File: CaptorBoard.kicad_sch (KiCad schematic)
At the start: 51 parts, among them J1 Conn_01x06-Connector, J2 Screw_Terminal_01x03, J3 Screw_Terminal_01x03, J4 Conn_01x07, J5 Conn_01x04, J6 Screw_Terminal_01x03, K1 G5LE-1-DC5, K2 G5LE-1-DC5, Q1 2N7002E, Q2 2N7002E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

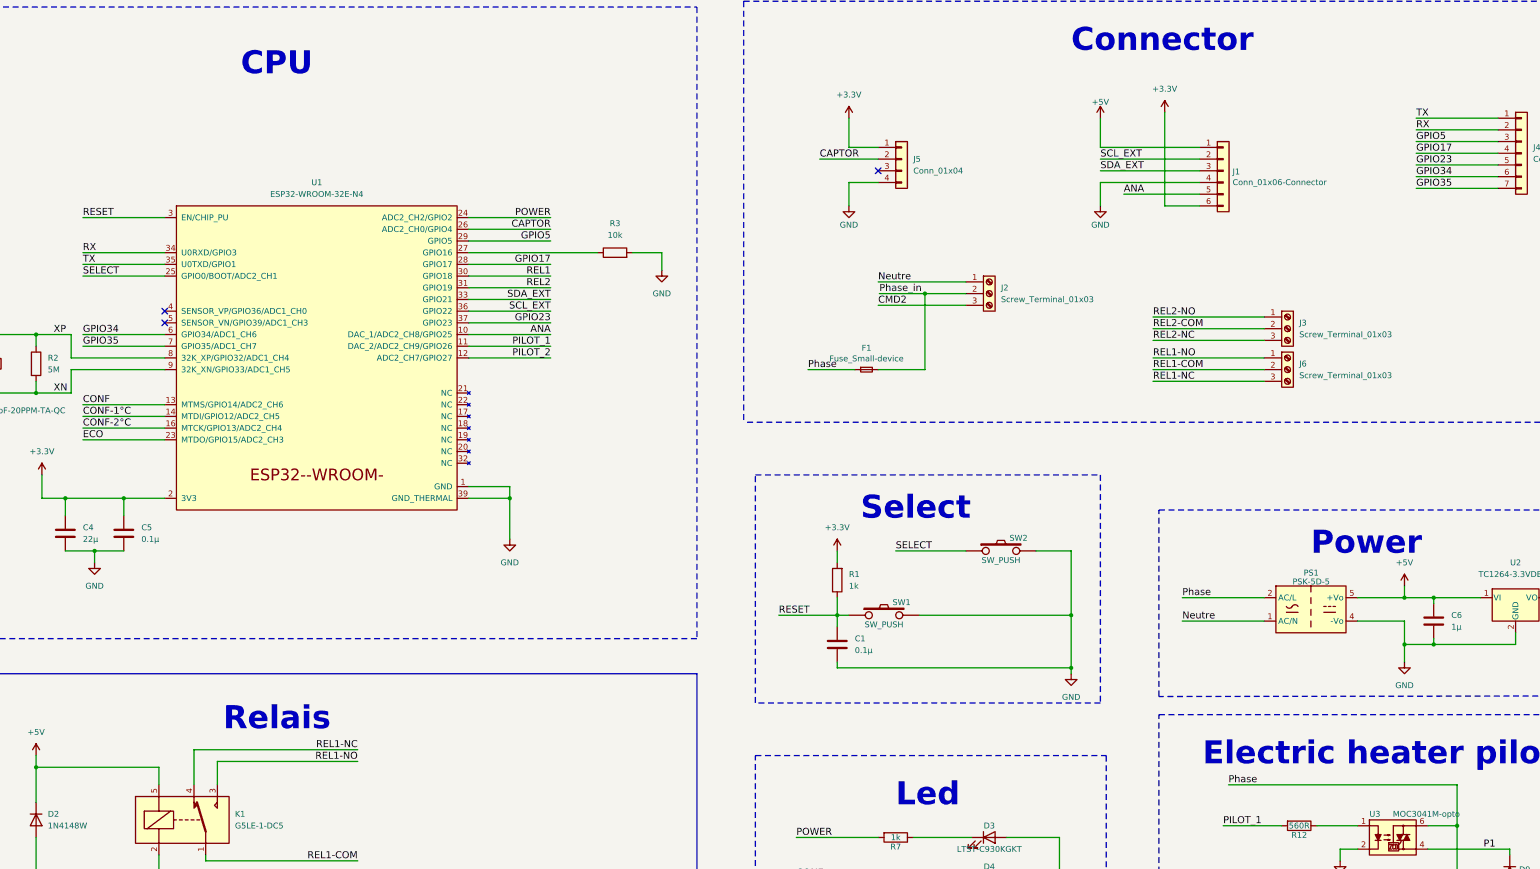
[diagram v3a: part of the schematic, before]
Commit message: Add two more anlog input and protect it
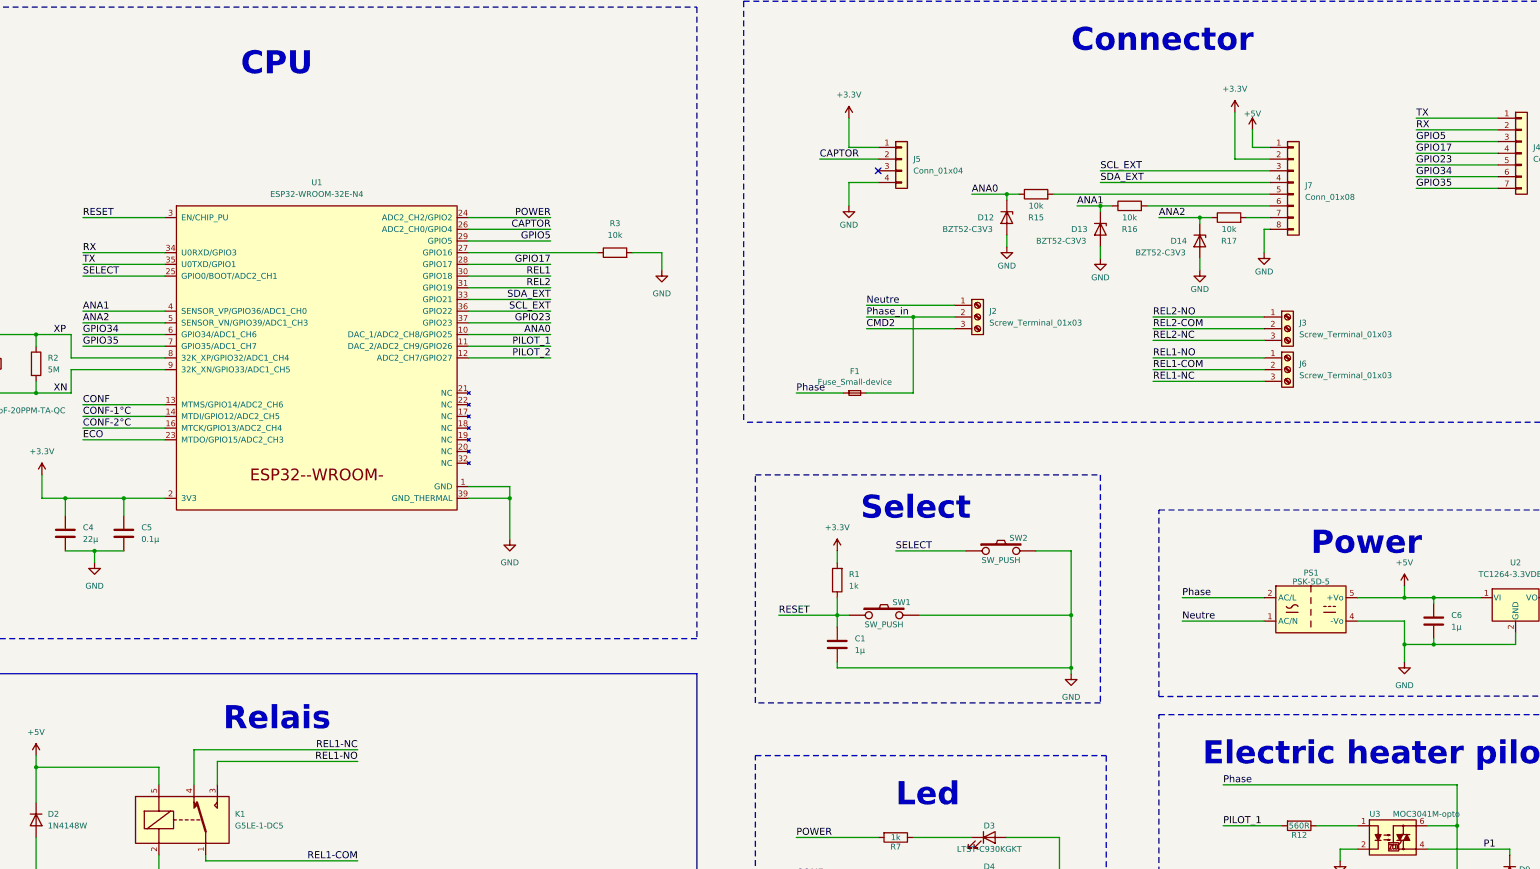
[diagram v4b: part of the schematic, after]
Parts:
- removed J1: Conn_01x06-Connector, Connector_PinHeader_2.54mm:PinHeader_1x06_P2.54mm_Vertical, symbol CaptorBoard-rescue:Conn_01x06-Connector
- added D12, D13, D14: BZT52-C3V3, Diode_SMD:D_SOD-123F, symbol Diode:BZT52Bxx
- added J7: Conn_01x08, Connector_PinHeader_2.54mm:PinHeader_1x08_P2.54mm_Vertical, symbol Connector_Generic:Conn_01x08
- added R15, R16, R17: 10k, Resistor_SMD:R_1210_3225Metric_Pad1.30x2.65mm_HandSolder, symbol Device:R
- C1: value 0.1µ -> 1µ; manf# 12101C104K4T2A -> CL32B105KBHNNNE
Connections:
- net +3.3V: now also J7.2 (Pin_2)
- net +5V: now also J7.1 (Pin_1)
- net GND: now also D12.2 (A), D13.2 (A), D14.2 (A), J7.8 (Pin_8)
- net SCL_EXT: now also J7.3 (Pin_3)
- net SDA_EXT: now also J7.4 (Pin_4)
- net ANA1: now reaches U1.4 (SENSOR_VP/GPIO36/ADC1_CH0)
- net ANA1: now also D13.1 (K), R16.1
- net ANA2: now reaches U1.5 (SENSOR_VN/GPIO39/ADC1_CH3)
- net ANA2: now also D14.1 (K), R17.1
- net ANA renamed ANA0
- net ANA0: now also D12.1 (K), R15.1
- new net: J7.7 (Pin_7), R17.2
- new net: J7.5 (Pin_5), R15.2
- new net: J7.6 (Pin_6), R16.2
- no-connect marks 3 -> 1
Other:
- moved on the sheet: F1, J2

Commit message: Change connecteur and pin for a better routing
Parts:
- removed J4: Conn_01x07, Connector_PinHeader_2.54mm:PinHeader_1x07_P2.54mm_Vertical, symbol Connector_Generic:Conn_01x07
- J7: footprint Connector_PinHeader_2.54mm:PinHeader_1x08_P2.54mm_Vertical -> Connector_PinHeader_2.54mm:PinHeader_2x08_P2.54mm_Vertical; symbol Connector_Generic:Conn_01x08 -> Connector_Generic:Conn_02x08_Odd_Even
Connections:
- net GPIO17 is gone; now on net CONF: U1.28 (GPIO17)
- net GPIO5 is gone; now on net CONF-1°C: U1.29 (GPIO5)
- net +3.3V: now also J7.1 (Pin_1); no longer J7.2 (Pin_2)
- net +5V: now also J7.2 (Pin_2), J7.3 (Pin_3); no longer J7.1 (Pin_1)
- net CONF: no longer U1.13 (MTMS/GPIO14/ADC2_CH6)
- net CONF-1°C: no longer U1.14 (MTDI/GPIO12/ADC2_CH5)
- net CONF-2°C: now also U1.30 (GPIO18); no longer U1.16 (MTCK/GPIO13/ADC2_CH4)
- net ECO: now also U1.31 (GPIO19); no longer U1.23 (MTDO/GPIO15/ADC2_CH3)
- net GND: now also J7.15 (Pin_15); no longer J7.8 (Pin_8)
- net GPIO23: now also J7.12 (Pin_12)
- net GPIO34: now also J7.8 (Pin_8)
- net GPIO35: now also J7.10 (Pin_10)
- net PILOT_1: now also U1.14 (MTDI/GPIO12/ADC2_CH5); no longer U1.11 (DAC_2/ADC2_CH9/GPIO26)
- net PILOT_2: now also U1.13 (MTMS/GPIO14/ADC2_CH6); no longer U1.12 (ADC2_CH7/GPIO27)
- net REL1: now also U1.16 (MTCK/GPIO13/ADC2_CH4); no longer U1.30 (GPIO18)
- net REL2: now also U1.23 (MTDO/GPIO15/ADC2_CH3); no longer U1.31 (GPIO19)
- net RX: now also J7.6 (Pin_6)
- net SCL_EXT: now also J7.5 (Pin_5); no longer J7.3 (Pin_3)
- net SDA_EXT: now also J7.7 (Pin_7); no longer J7.4 (Pin_4)
- net TX: now also J7.4 (Pin_4)
- net at R17.2: now also J7.13 (Pin_13); no longer J7.7 (Pin_7)
- net at R15.2: now also J7.9 (Pin_9); no longer J7.5 (Pin_5)
- net at R16.2: now also J7.11 (Pin_11); no longer J7.6 (Pin_6)
- new net GPIO26: J7.14 (Pin_14), U1.11 (DAC_2/ADC2_CH9/GPIO26)
- new net GPIO27: J7.16 (Pin_16), U1.12 (ADC2_CH7/GPIO27)

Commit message: add CEM protection, and change reférance for Digikey distributor
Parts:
- added R18: 12, Resistor_SMD:R_2512_6332Metric_Pad1.40x3.35mm_HandSolder, symbol Device:R
- added RV1: B72210S0351K101, Varistor:RV_Disc_D12mm_W5.1mm_P7.5mm, symbol Device:Varistor
- C2, C3: footprint Capacitor_SMD:C_1210_3225Metric_Pad1.33x2.70mm_HandSolder -> Capacitor_SMD:C_1206_3216Metric_Pad1.33x1.80mm_HandSolder; manf# C1210C120J1HACTU -> C1206C120J5GAC7800
- D10, D9: manf# 1N4004T-G -> 1N4004RLG
- F1: manf# 0443001.DR -> 3405.0166.11
- PS1: value PSK-5D-5 -> LD03-23B05R2; manf# PSK-5D-5 -> LD03-23B05R2
- Q1, Q2: manf# 2N7002E-7-F -> T2N7002BK\,LM
- R1, R10, R11, R14, R5, R7, R8, R9: manf# RMC1/4-102JTE -> RMCF1210JT1K00
- SW1, SW2: manf# SKHHLPA010 -> TL1105VF100Q
- U1: value ESP32-WROOM-32E-N4 -> ESP32-WROOM-32E-H4; manf# ESP32-WROOM-32E-N4 -> ESP32-WROOM-32E-H4
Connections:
- net Neutre: now also RV1.2
- net Phase: now also R18.1, RV1.1; no longer PS1.2 (AC/L)
- new net Phase_f: PS1.2 (AC/L), R18.2
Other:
- moved on the sheet: C1, C6, D10, D12, D13, D14, D3, D4, D5, D6, D7, D9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

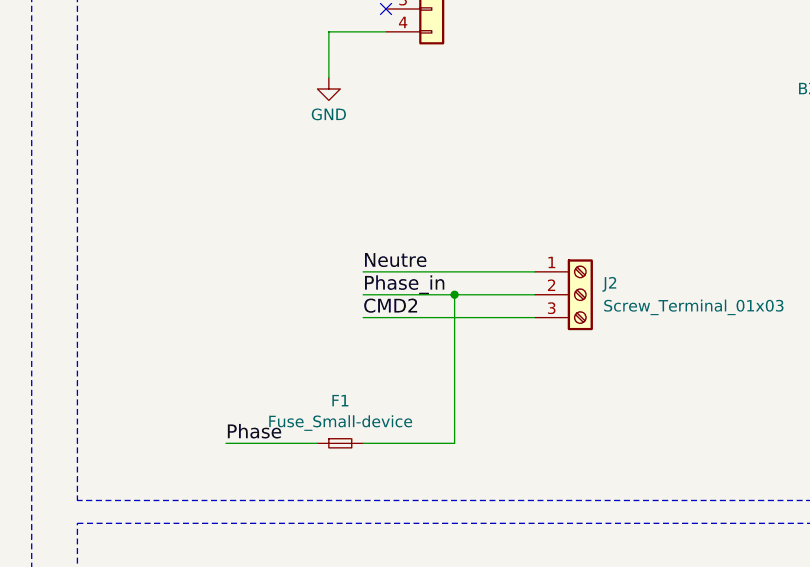
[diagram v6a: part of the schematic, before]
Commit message: change a bad foot print for fuse
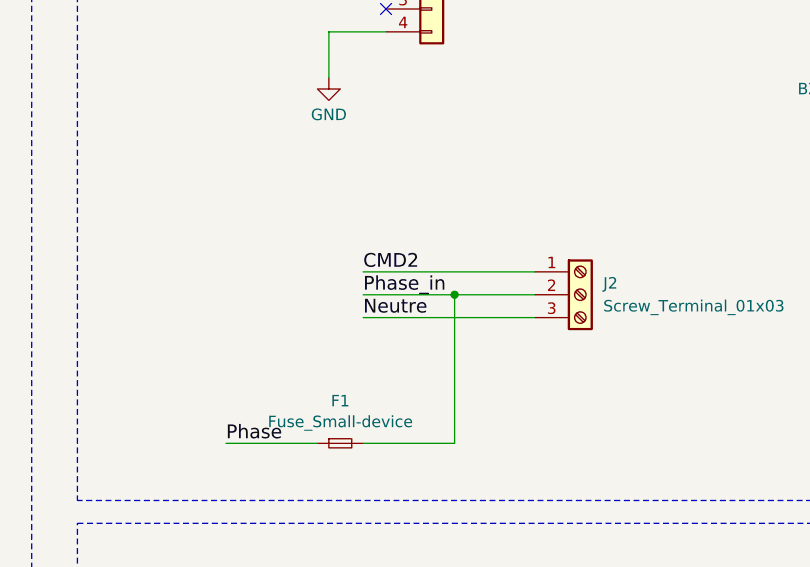
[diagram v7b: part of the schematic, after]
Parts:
- F1: footprint Fuse:Fuseholder_Littelfuse_Nano2_157x -> Fuse:Fuse_Schurter_UMT250
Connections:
- net CMD2: now also J2.1 (Pin_1); no longer J2.3 (Pin_3)
- net Neutre: now also J2.3 (Pin_3); no longer J2.1 (Pin_1)

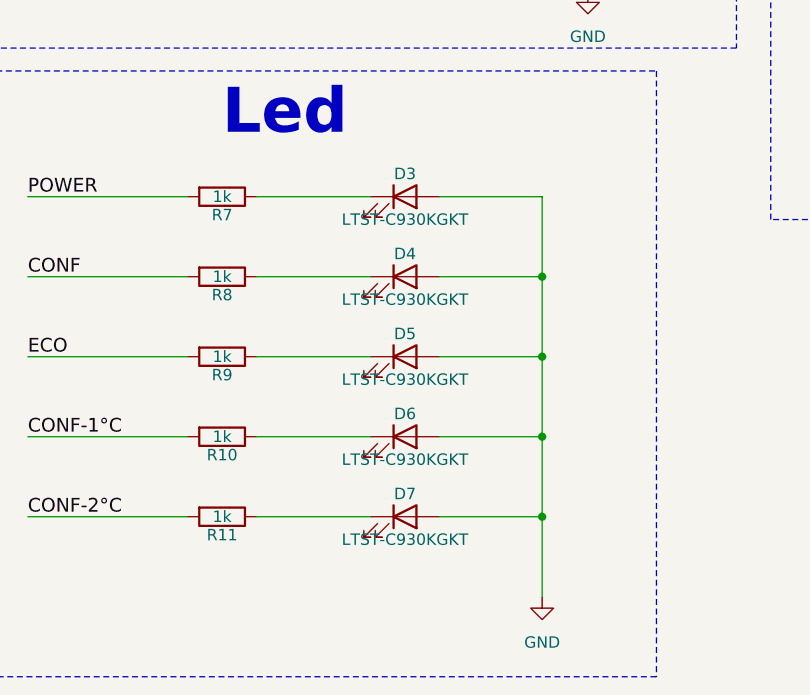
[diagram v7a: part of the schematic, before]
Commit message: LED it inversed
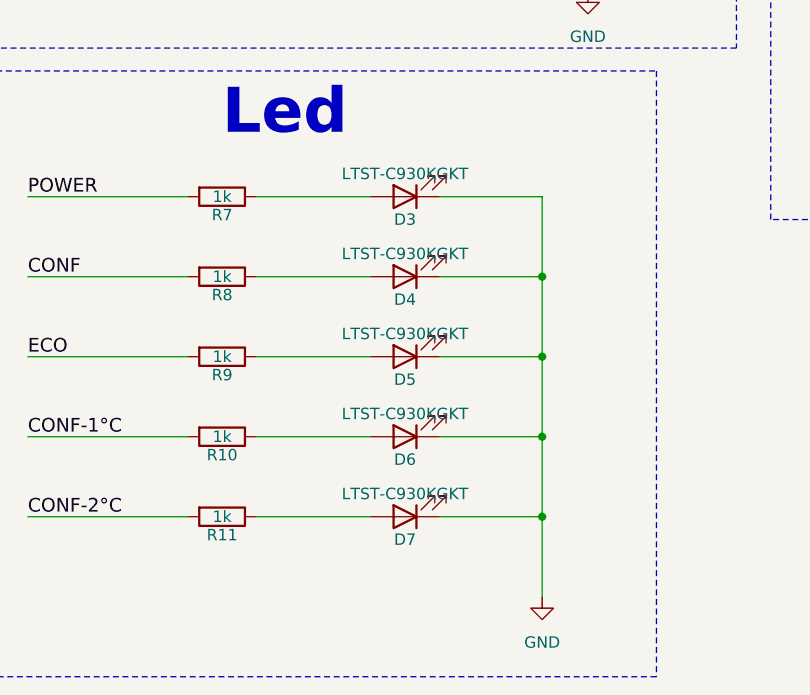
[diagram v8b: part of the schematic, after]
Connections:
- net GND: now also D3.1 (K), D4.1 (K), D5.1 (K), D6.1 (K), D7.1 (K); no longer D3.2 (A), D4.2 (A), D5.2 (A), D6.2 (A), D7.2 (A)
- net at R7.1: now also D3.2 (A); no longer D3.1 (K)
- net at R8.1: now also D4.2 (A); no longer D4.1 (K)
- net at R9.1: now also D5.2 (A); no longer D5.1 (K)
- net at R10.1: now also D6.2 (A); no longer D6.1 (K)
- net at R11.1: now also D7.2 (A); no longer D7.1 (K)
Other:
- moved on the sheet: D3, D4, D5, D6, D7
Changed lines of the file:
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@@
     (effects (font (size 1.524 1.524)) (justify left bottom))
   )
-  (symbol (lib_id "Device:LED") (at 260.35 227.33 0) (unit 1)
+  (symbol (lib_id "Device:LED") (at 260.35 227.33 180) (unit 1)
     (in_bom yes) (on_board yes) (dnp no)
-    (property "Reference" "D3" (at 260.35 224.79 0)
+    (property "Reference" "D3" (at 260.35 229.87 0)
       (effects (font (size 1.27 1.27)))
     )
-    (property "Value" "LTST-C930KGKT" (at 260.35 229.87 0)
+    (property "Value" "LTST-C930KGKT" (at 260.35 224.79 0)
       (effects (font (size 1.27 1.27)))
     )
@@
     )
   )
-  (symbol (lib_id "Device:LED") (at 260.35 236.22 0) (unit 1)
+  (symbol (lib_id "Device:LED") (at 260.35 236.22 180) (unit 1)
     (in_bom yes) (on_board yes) (dnp no)
-    (property "Reference" "D4" (at 260.35 233.68 0)
+    (property "Reference" "D4" (at 260.35 238.76 0)
       (effects (font (size 1.27 1.27)))
     )
-    (property "Value" "LTST-C930KGKT" (at 260.35 238.76 0)
+    (property "Value" "LTST-C930KGKT" (at 260.35 233.68 0)
       (effects (font (size 1.27 1.27)))
     )
@@
     )
   )
-  (symbol (lib_id "Device:LED") (at 260.35 245.11 0) (unit 1)
+  (symbol (lib_id "Device:LED") (at 260.35 245.11 180) (unit 1)
     (in_bom yes) (on_board yes) (dnp no)
-    (property "Reference" "D5" (at 260.35 242.57 0)
+    (property "Reference" "D5" (at 260.35 247.65 0)
       (effects (font (size 1.27 1.27)))
     )
-    (property "Value" "LTST-C930KGKT" (at 260.35 247.65 0)
+    (property "Value" "LTST-C930KGKT" (at 260.35 242.57 0)
       (effects (font (size 1.27 1.27)))
     )
@@
     )
   )
-  (symbol (lib_id "Device:LED") (at 260.35 254 0) (unit 1)
+  (symbol (lib_id "Device:LED") (at 260.35 254 180) (unit 1)
     (in_bom yes) (on_board yes) (dnp no)
-    (property "Reference" "D6" (at 260.35 251.46 0)
+    (property "Reference" "D6" (at 260.35 256.54 0)
       (effects (font (size 1.27 1.27)))
     )
-    (property "Value" "LTST-C930KGKT" (at 260.35 256.54 0)
+    (property "Value" "LTST-C930KGKT" (at 260.35 251.46 0)
       (effects (font (size 1.27 1.27)))
     )
@@
     )
   )
-  (symbol (lib_id "Device:LED") (at 260.35 262.89 0) (unit 1)
+  (symbol (lib_id "Device:LED") (at 260.35 262.89 180) (unit 1)
     (in_bom yes) (on_board yes) (dnp no)
-    (property "Reference" "D7" (at 260.35 260.35 0)
+    (property "Reference" "D7" (at 260.35 265.43 0)
       (effects (font (size 1.27 1.27)))
     )
-    (property "Value" "LTST-C930KGKT" (at 260.35 265.43 0)
+    (property "Value" "LTST-C930KGKT" (at 260.35 260.35 0)
       (effects (font (size 1.27 1.27)))
     )
